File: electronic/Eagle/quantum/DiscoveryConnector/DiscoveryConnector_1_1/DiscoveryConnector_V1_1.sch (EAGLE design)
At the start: 4 parts, among them J1 686104183422, J2 686104183422

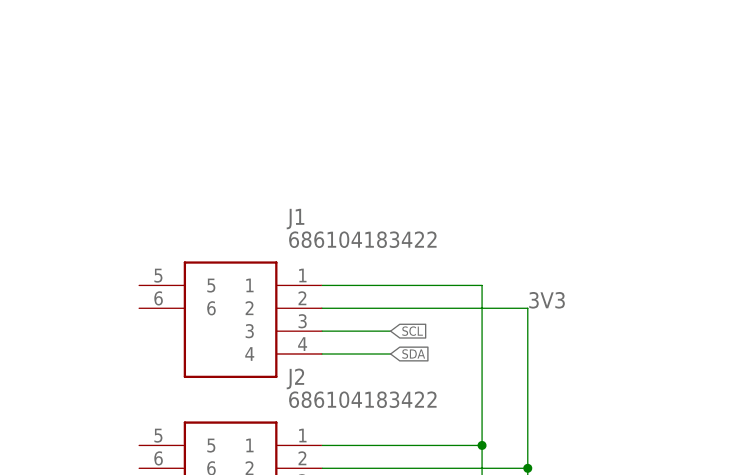
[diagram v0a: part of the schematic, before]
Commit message: finished all boards s for next PCBway production
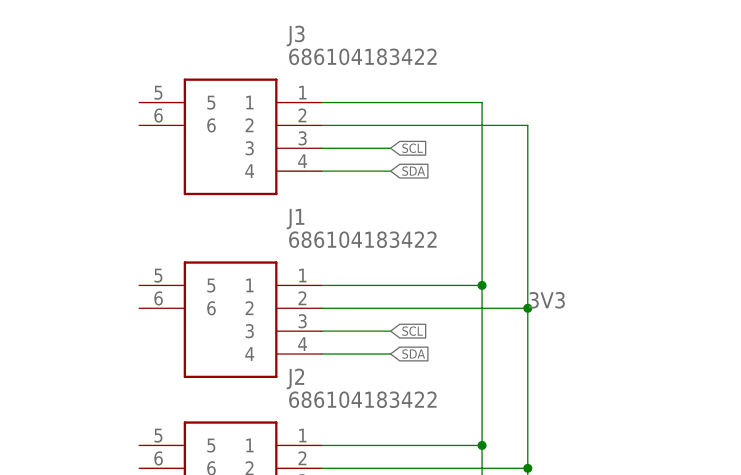
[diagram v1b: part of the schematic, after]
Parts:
- added J3: 686104183422, electro_mechanical:686104183422
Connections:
- net 3V3: now also J3.2
- net GND: now also J3.1
- net SCL: now also J3.3
- net SDA: now also J3.4
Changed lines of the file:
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@@
 </classes>
 <parts>
-<part name="B1" library="electro_mechanical" library_urn="urn:adsk.eagle:library:16388331" deviceset="ARDUINO_UNO_R3" device="" package3d_urn="urn:adsk.eagle:package:17310799/2"/>
-<part name="DISPLAY" library="electro_mechanical" library_urn="urn:adsk.eagle:library:16388331" deviceset="90814-0204" device="" package3d_urn="urn:adsk.eagle:package:16762552/3"/>
+<part name="B1" library="electro_mechanical" library_urn="urn:adsk.eagle:library:16388331" deviceset="ARDUINO_UNO_R3" device="" package3d_urn="urn:adsk.eagle:package:17310799/4"/>
+<part name="DISPLAY" library="electro_mechanical" library_urn="urn:adsk.eagle:library:16388331" deviceset="90814-0204" device="" package3d_urn="urn:adsk.eagle:package:16762552/4"/>
 <part name="SUPPLY1" library="supply2" library_urn="urn:adsk.eagle:library:372" deviceset="GND" device=""/>
 <part name="SUPPLY2" library="supply2" library_urn="urn:adsk.eagle:library:372" deviceset="GND" device=""/>
@@
 <part name="J1" library="electro_mechanical" library_urn="urn:adsk.eagle:library:16388331" deviceset="686104183422" device="" package3d_urn="urn:adsk.eagle:package:18115753/3"/>
 <part name="J2" library="electro_mechanical" library_urn="urn:adsk.eagle:library:16388331" deviceset="686104183422" device="" package3d_urn="urn:adsk.eagle:package:18115753/3"/>
+<part name="J3" library="electro_mechanical" library_urn="urn:adsk.eagle:library:16388331" deviceset="686104183422" device="" package3d_urn="urn:adsk.eagle:package:18115753/3"/>
 </parts>
 <sheets>
@@
 <attribute name="NAME" x="57.15" y="96.52" size="1.778" layer="95" align="center-left"/>
 <attribute name="VALUE" x="57.15" y="93.98" size="1.778" layer="96" align="center-left"/>
+</instance>
+<instance part="J3" gate="G$1" x="40.64" y="127" smashed="yes">
+<attribute name="NAME" x="57.15" y="134.62" size="1.778" layer="95" align="center-left"/>
+<attribute name="VALUE" x="57.15" y="132.08" size="1.778" layer="96" align="center-left"/>
 </instance>
 </instances>
@@
 <wire x1="60.96" y1="88.9" x2="78.74" y2="88.9" width="0.1524" layer="91"/>
 <junction x="78.74" y="88.9"/>
+<pinref part="J3" gate="G$1" pin="1"/>
+<wire x1="78.74" y1="127" x2="60.96" y2="127" width="0.1524" layer="91"/>
+<wire x1="78.74" y1="106.68" x2="78.74" y2="127" width="0.1524" layer="91"/>
+<junction x="78.74" y="106.68"/>
 </segment>
 </net>
@@
 </segment>
 </net>
-<net name="3V3" class="0">
-<segment>
-<pinref part="B1" gate="G$1" pin="3.3V"/>
-<wire x1="91.44" y1="50.8" x2="83.82" y2="50.8" width="0.1524" layer="91"/>
-<wire x1="83.82" y1="50.8" x2="83.82" y2="86.36" width="0.1524" layer="91"/>
-<label x="83.82" y="104.14" size="1.778" layer="95"/>
-<pinref part="J1" gate="G$1" pin="2"/>
-<wire x1="83.82" y1="86.36" x2="83.82" y2="104.14" width="0.1524" layer="91"/>
-<wire x1="83.82" y1="104.14" x2="60.96" y2="104.14" width="0.1524" layer="91"/>
-<pinref part="J2" gate="G$1" pin="2"/>
-<wire x1="60.96" y1="86.36" x2="83.82" y2="86.36" width="0.1524" layer="91"/>
-<junction x="83.82" y="86.36"/>
-</segment>
-</net>
 <net name="SDA" class="0">
 <segment>
@@
 <wire x1="60.96" y1="81.28" x2="63.5" y2="81.28" width="0.1524" layer="91"/>
 <pinref part="J2" gate="G$1" pin="4"/>
+</segment>
+<segment>
+<label x="68.58" y="119.38" size="1.016" layer="95" rot="MR180" xref="yes"/>
+<pinref part="J3" gate="G$1" pin="4"/>
+<wire x1="60.96" y1="119.38" x2="68.58" y2="119.38" width="0.1524" layer="91"/>
 </segment>
 </net>
@@
 <pinref part="J2" gate="G$1" pin="3"/>
 </segment>
+<segment>
+<label x="68.58" y="121.92" size="1.016" layer="95" rot="MR180" xref="yes"/>
+<pinref part="J3" gate="G$1" pin="3"/>
+<wire x1="68.58" y1="121.92" x2="60.96" y2="121.92" width="0.1524" layer="91"/>
+</segment>
 </net>
+<net name="3V3" class="0">
+<segment>
+<pinref part="J3" gate="G$1" pin="2"/>
+<wire x1="83.82" y1="124.46" x2="60.96" y2="124.46" width="0.1524" layer="91"/>
+<pinref part="B1" gate="G$1" pin="3.3V"/>
+<wire x1="91.44" y1="50.8" x2="83.82" y2="50.8" width="0.1524" layer="91"/>
+<wire x1="83.82" y1="50.8" x2="83.82" y2="86.36" width="0.1524" layer="91"/>
+<label x="83.82" y="104.14" size="1.778" layer="95"/>
+<pinref part="J1" gate="G$1" pin="2"/>
+<wire x1="83.82" y1="86.36" x2="83.82" y2="104.14" width="0.1524" layer="91"/>
+<wire x1="83.82" y1="104.14" x2="60.96" y2="104.14" width="0.1524" layer="91"/>
+<pinref part="J2" gate="G$1" pin="2"/>
+<wire x1="60.96" y1="86.36" x2="83.82" y2="86.36" width="0.1524" layer="91"/>
+<junction x="83.82" y="86.36"/>
+<wire x1="83.82" y1="124.46" x2="83.82" y2="104.14" width="0.1524" layer="91"/>
+<junction x="83.82" y="104.14"/>
+</segment>
+</net>
